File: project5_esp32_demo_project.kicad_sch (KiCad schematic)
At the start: 25 parts, among them J1 SS-52400-002, J2 B2B-PH-SM4-TB, U1 MCP73871-2CAI_ML

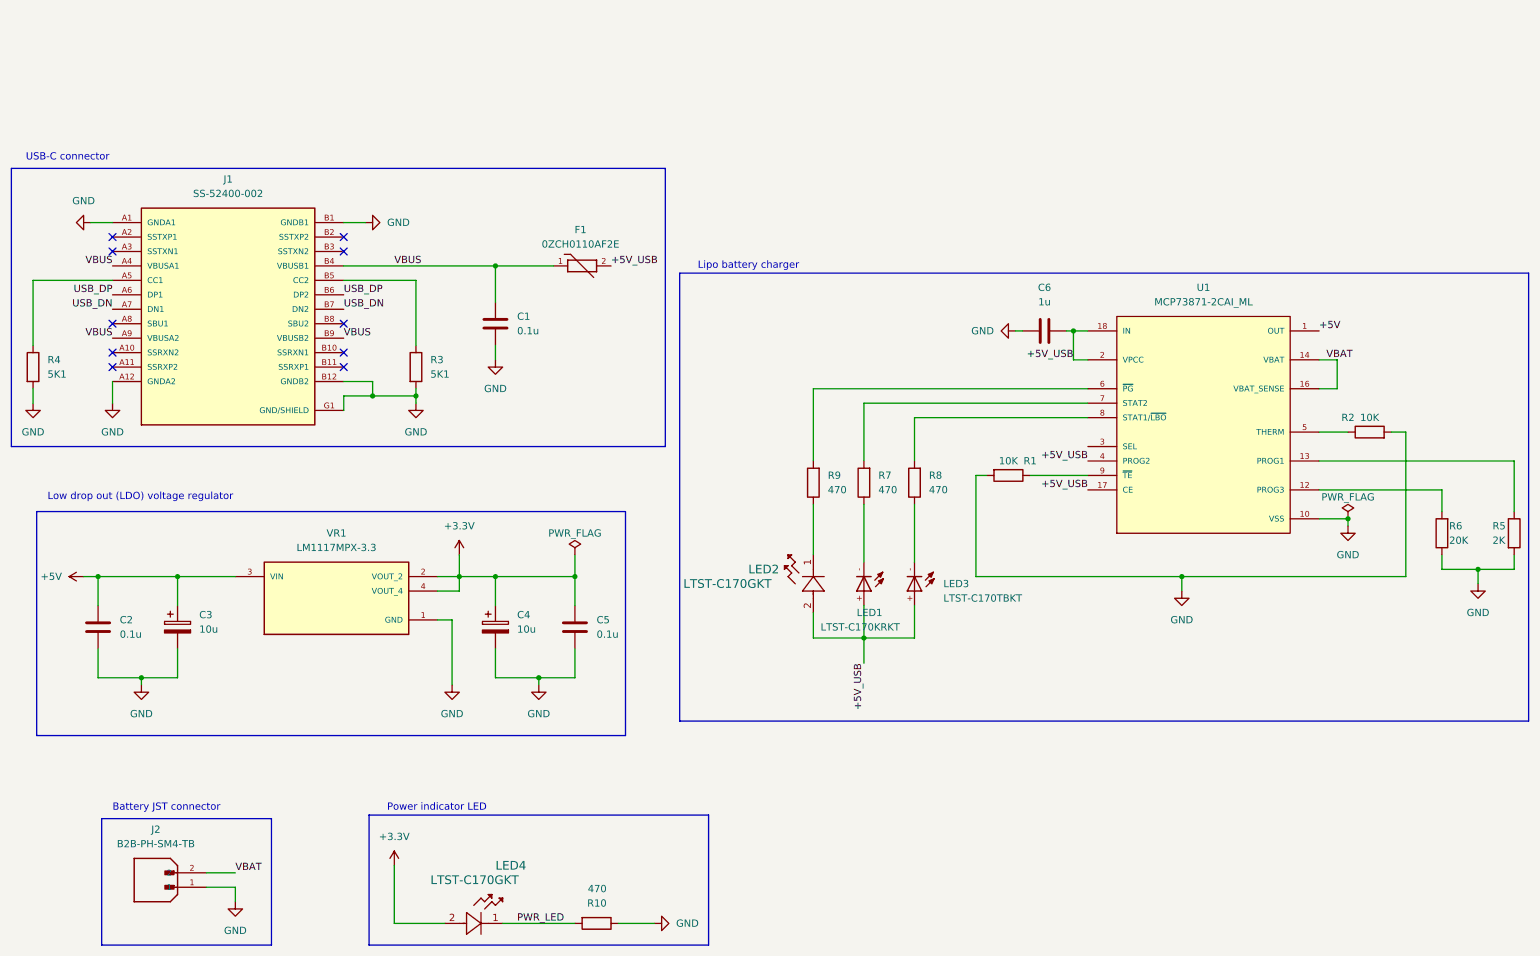
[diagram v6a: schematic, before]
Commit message: 1.1.8 Add a hierarchical sheet symbol to page 2
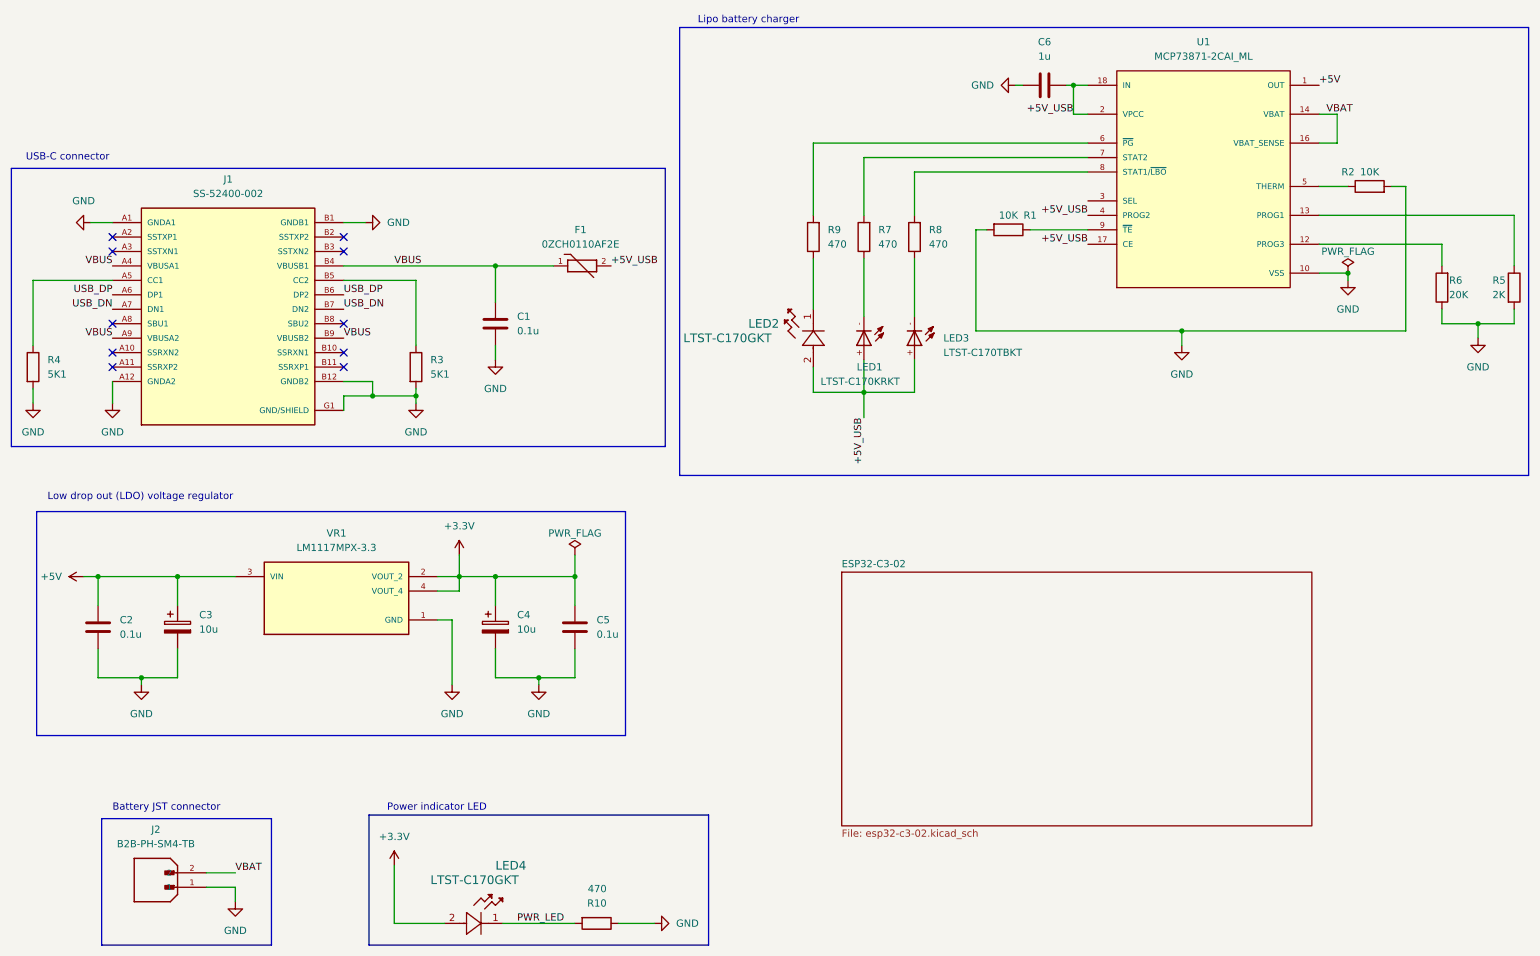
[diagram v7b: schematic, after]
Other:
- added sheet ESP32-C3-02 (esp32-c3-02.kicad_sch)
- moved on the sheet: C6, LED1, LED2, LED3, R1, R2, R5, R6, R7, R8, R9, U1

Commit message: 1.1.9 Finish work in sheet 1
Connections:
- net at LED2.1: now also R7.1; no longer R9.1
- net at LED1.-: now also R8.1; no longer R7.1
- net CHARGED: now reaches R7.2, U1.7 (STAT2)
- net CHARGING_POWER_GOOD: now reaches R9.2, U1.6 (~{PG})
- net at LED3.-: now also R9.1; no longer R8.1
- net CHARGING: now reaches R8.2, U1.8 (STAT1/~{LBO})
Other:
- moved on the sheet: LED1, LED2, LED3, R8, R9
